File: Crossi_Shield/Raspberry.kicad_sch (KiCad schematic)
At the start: 12 parts, among them J1 Raspberry_Pi_2_3, SW1 SW_DIP_x01

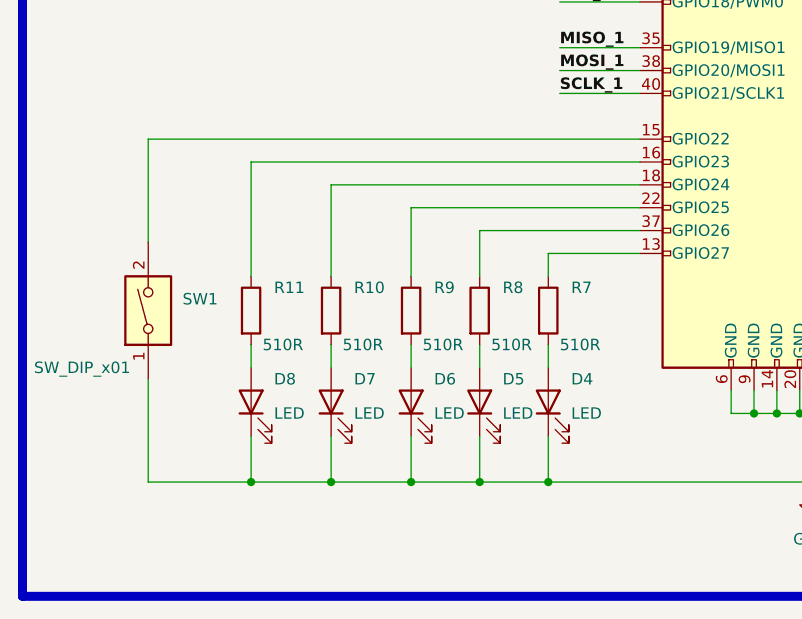
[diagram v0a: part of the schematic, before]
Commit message: new buckconf design
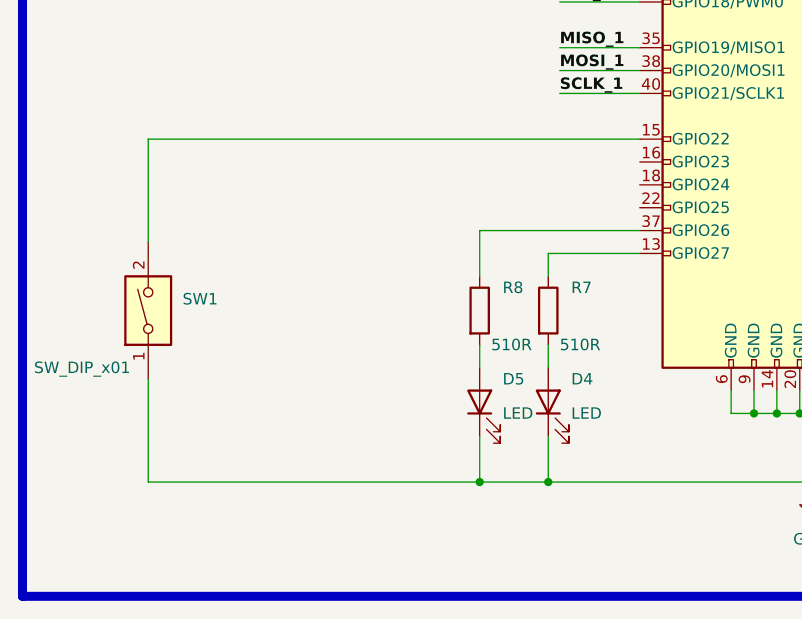
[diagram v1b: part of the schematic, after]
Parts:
- removed D6, D7, D8: LED, LED_SMD:LED_0805_2012Metric_Pad1.15x1.40mm_HandSolder, symbol Device:LED
- removed R10, R11, R9: 510R, Resistor_SMD:R_0805_2012Metric_Pad1.20x1.40mm_HandSolder, symbol Device:R
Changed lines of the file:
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@@
   (junction (at 99.06 138.43) (diameter 0) (color 0 0 0 0)
   )
-  (junction (at 74.93 138.43) (diameter 0) (color 0 0 0 0)
-  )
   (junction (at 127 130.81) (diameter 0) (color 0 0 0 0)
   )
-  (junction (at 66.04 138.43) (diameter 0) (color 0 0 0 0)
-  )
   (junction (at 124.46 130.81) (diameter 0) (color 0 0 0 0)
   )
@@
   (junction (at 128.27 130.81) (diameter 0) (color 0 0 0 0)
   )
-  (junction (at 83.82 138.43) (diameter 0) (color 0 0 0 0)
-  )
   (junction (at 121.92 130.81) (diameter 0) (color 0 0 0 0)
   )
@@
   (junction (at 129.54 130.81) (diameter 0) (color 0 0 0 0)
   )
-  (wire (pts (xy 109.22 105.41) (xy 74.93 105.41))
-    (stroke (width 0) (type default))
-  )
   (wire (pts (xy 223.52 78.74) (xy 232.41 78.74))
     (stroke (width 0) (type default))
@@
     (stroke (width 0) (type default))
   )
-  (wire (pts (xy 66.04 138.43) (xy 74.93 138.43))
-    (stroke (width 0) (type default))
-  )
   (wire (pts (xy 200.66 78.74) (xy 210.82 78.74))
     (stroke (width 0) (type default))
   )
-  (wire (pts (xy 83.82 107.95) (xy 83.82 115.57))
-    (stroke (width 0) (type default))
-  )
   (wire (pts (xy 223.52 86.36) (xy 232.41 86.36))
     (stroke (width 0) (type default))
@@
     (stroke (width 0) (type default))
   )
-  (wire (pts (xy 74.93 138.43) (xy 83.82 138.43))
-    (stroke (width 0) (type default))
-  )
   (wire (pts (xy 200.66 86.36) (xy 207.01 86.36))
     (stroke (width 0) (type default))
@@
     (stroke (width 0) (type default))
   )
-  (wire (pts (xy 83.82 123.19) (xy 83.82 125.73))
-    (stroke (width 0) (type default))
-  )
-  (wire (pts (xy 83.82 138.43) (xy 91.44 138.43))
+  (wire (pts (xy 54.61 138.43) (xy 91.44 138.43))
     (stroke (width 0) (type default))
   )
@@
     (stroke (width 0) (type default))
   )
-  (wire (pts (xy 66.04 123.19) (xy 66.04 125.73))
-    (stroke (width 0) (type default))
-  )
-  (wire (pts (xy 83.82 133.35) (xy 83.82 138.43))
-    (stroke (width 0) (type default))
-  )
-  (wire (pts (xy 54.61 138.43) (xy 66.04 138.43))
-    (stroke (width 0) (type default))
-  )
   (wire (pts (xy 149.86 100.33) (xy 158.75 100.33))
     (stroke (width 0) (type default))
@@
     (stroke (width 0) (type default))
   )
-  (wire (pts (xy 74.93 105.41) (xy 74.93 115.57))
-    (stroke (width 0) (type default))
-  )
   (wire (pts (xy 149.86 97.79) (xy 158.75 97.79))
     (stroke (width 0) (type default))
@@
     (stroke (width 0) (type default))
   )
-  (wire (pts (xy 74.93 123.19) (xy 74.93 125.73))
-    (stroke (width 0) (type default))
-  )
   (wire (pts (xy 149.86 80.01) (xy 156.21 80.01))
     (stroke (width 0) (type default))
@@
     (stroke (width 0) (type default))
   )
-  (wire (pts (xy 66.04 133.35) (xy 66.04 138.43))
-    (stroke (width 0) (type default))
-  )
   (wire (pts (xy 134.62 128.27) (xy 134.62 130.81))
     (stroke (width 0) (type default))
@@
     (stroke (width 0) (type default))
   )
-  (wire (pts (xy 109.22 107.95) (xy 83.82 107.95))
-    (stroke (width 0) (type default))
-  )
   (wire (pts (xy 200.66 68.58) (xy 207.01 68.58))
     (stroke (width 0) (type default))
@@
     (stroke (width 0) (type default))
   )
-  (wire (pts (xy 66.04 102.87) (xy 66.04 115.57))
-    (stroke (width 0) (type default))
-  )
   (wire (pts (xy 124.46 128.27) (xy 124.46 130.81))
     (stroke (width 0) (type default))
@@
     (stroke (width 0) (type default))
   )
-  (wire (pts (xy 109.22 102.87) (xy 66.04 102.87))
-    (stroke (width 0) (type default))
-  )
   (wire (pts (xy 149.86 72.39) (xy 156.21 72.39))
     (stroke (width 0) (type default))
@@
   )
   (wire (pts (xy 99.06 138.43) (xy 128.27 138.43))
-    (stroke (width 0) (type default))
-  )
-  (wire (pts (xy 74.93 133.35) (xy 74.93 138.43))
     (stroke (width 0) (type default))
   )
@@
         (path "/da1a3662-bd33-45fa-9d2c-eaee6b865c8d/f28ea0f3-753b-42f3-99ad-0aa8f46314aa"
           (reference "D5") (unit 1)
-        )
-      )
-    )
-  )
-  (symbol (lib_id "Device:R") (at 74.93 119.38 0) (unit 1)
-    (in_bom yes) (on_board yes) (dnp no)
-    (property "Reference" "R10" (at 77.47 116.84 0)
-      (effects (font (size 1.27 1.27)) (justify left))
-    )
-    (property "Value" "510R" (at 76.2 123.19 0)
-      (effects (font (size 1.27 1.27)) (justify left))
-    )
-    (property "Footprint" "Resistor_SMD:R_0805_2012Metric_Pad1.20x1.40mm_HandSolder" (at 73.152 119.38 90)
-      (effects (font (size 1.27 1.27)) hide)
-    )
-    (property "Datasheet" "~" (at 74.93 119.38 0)
-      (effects (font (size 1.27 1.27)) hide)
-    )
-    (pin "1")
-    (pin "2")
-    (instances
-      (project "Crossi_Shield"
-        (path "/da1a3662-bd33-45fa-9d2c-eaee6b865c8d/f28ea0f3-753b-42f3-99ad-0aa8f46314aa"
-          (reference "R10") (unit 1)
         )
       )
@@
     )
   )
-  (symbol (lib_id "Device:LED") (at 74.93 129.54 90) (unit 1)
-    (in_bom yes) (on_board yes) (dnp no)
-    (property "Reference" "D7" (at 77.47 127 90)
-      (effects (font (size 1.27 1.27)) (justify right))
-    )
-    (property "Value" "LED" (at 77.47 130.81 90)
-      (effects (font (size 1.27 1.27)) (justify right))
-    )
-    (property "Footprint" "LED_SMD:LED_0805_2012Metric_Pad1.15x1.40mm_HandSolder" (at 74.93 129.54 0)
-      (effects (font (size 1.27 1.27)) hide)
-    )
-    (property "Datasheet" "~" (at 74.93 129.54 0)
-      (effects (font (size 1.27 1.27)) hide)
-    )
-    (pin "1")
-    (pin "2")
-    (instances
-      (project "Crossi_Shield"
-        (path "/da1a3662-bd33-45fa-9d2c-eaee6b865c8d/f28ea0f3-753b-42f3-99ad-0aa8f46314aa"
-          (reference "D7") (unit 1)
-        )
-      )
-    )
-  )
-  (symbol (lib_id "Device:R") (at 83.82 119.38 0) (unit 1)
-    (in_bom yes) (on_board yes) (dnp no)
-    (property "Reference" "R9" (at 86.36 116.84 0)
-      (effects (font (size 1.27 1.27)) (justify left))
-    )
-    (property "Value" "510R" (at 85.09 123.19 0)
-      (effects (font (size 1.27 1.27)) (justify left))
-    )
-    (property "Footprint" "Resistor_SMD:R_0805_2012Metric_Pad1.20x1.40mm_HandSolder" (at 82.042 119.38 90)
-      (effects (font (size 1.27 1.27)) hide)
-    )
-    (property "Datasheet" "~" (at 83.82 119.38 0)
-      (effects (font (size 1.27 1.27)) hide)
-    )
-    (pin "1")
-    (pin "2")
-    (instances
-      (project "Crossi_Shield"
-        (path "/da1a3662-bd33-45fa-9d2c-eaee6b865c8d/f28ea0f3-753b-42f3-99ad-0aa8f46314aa"
-          (reference "R9") (unit 1)
-        )
-      )
-    )
-  )
-  (symbol (lib_id "Device:LED") (at 83.82 129.54 90) (unit 1)
-    (in_bom yes) (on_board yes) (dnp no)
-    (property "Reference" "D6" (at 86.36 127 90)
-      (effects (font (size 1.27 1.27)) (justify right))
-    )
-    (property "Value" "LED" (at 86.36 130.81 90)
-      (effects (font (size 1.27 1.27)) (justify right))
-    )
-    (property "Footprint" "LED_SMD:LED_0805_2012Metric_Pad1.15x1.40mm_HandSolder" (at 83.82 129.54 0)
-      (effects (font (size 1.27 1.27)) hide)
-    )
-    (property "Datasheet" "~" (at 83.82 129.54 0)
-      (effects (font (size 1.27 1.27)) hide)
-    )
-    (pin "1")
-    (pin "2")
-    (instances
-      (project "Crossi_Shield"
-        (path "/da1a3662-bd33-45fa-9d2c-eaee6b865c8d/f28ea0f3-753b-42f3-99ad-0aa8f46314aa"
-          (reference "D6") (unit 1)
-        )
-      )
-    )
-  )
   (symbol (lib_id "Device:R") (at 99.06 119.38 0) (unit 1)
     (in_bom yes) (on_board yes) (dnp no)
@@
     )
   )
-  (symbol (lib_id "Device:LED") (at 66.04 129.54 90) (unit 1)
-    (in_bom yes) (on_board yes) (dnp no)
-    (property "Reference" "D8" (at 68.58 127 90)
-      (effects (font (size 1.27 1.27)) (justify right))
-    )
-    (property "Value" "LED" (at 68.58 130.81 90)
-      (effects (font (size 1.27 1.27)) (justify right))
-    )
-    (property "Footprint" "LED_SMD:LED_0805_2012Metric_Pad1.15x1.40mm_HandSolder" (at 66.04 129.54 0)
-      (effects (font (size 1.27 1.27)) hide)
-    )
-    (property "Datasheet" "~" (at 66.04 129.54 0)
-      (effects (font (size 1.27 1.27)) hide)
-    )
-    (pin "1")
-    (pin "2")
-    (instances
-      (project "Crossi_Shield"
-        (path "/da1a3662-bd33-45fa-9d2c-eaee6b865c8d/f28ea0f3-753b-42f3-99ad-0aa8f46314aa"
-          (reference "D8") (unit 1)
-        )
-      )
-    )
-  )
   (symbol (lib_id "Switch:SW_DIP_x01") (at 54.61 119.38 90) (unit 1)
     (in_bom yes) (on_board yes) (dnp no)
@@
         )
       )
-    )
-  )
-  (symbol (lib_id "Device:R") (at 66.04 119.38 0) (unit 1)
-    (in_bom yes) (on_board yes) (dnp no)
-    (property "Reference" "R11" (at 68.58 116.84 0)
-      (effects (font (size 1.27 1.27)) (justify left))
-    )
-    (property "Value" "510R" (at 67.31 123.19 0)
-      (effects (font (size 1.27 1.27)) (justify left))
-    )
-    (property "Footprint" "Resistor_SMD:R_0805_2012Metric_Pad1.20x1.40mm_HandSolder" (at 64.262 119.38 90)
-      (effects (font (size 1.27 1.27)) hide)
-    )
-    (property "Datasheet" "~" (at 66.04 119.38 0)
-      (effects (font (size 1.27 1.27)) hide)
-    )
-    (pin "1")
-    (pin "2")
-    (instances
-      (project "Crossi_Shield"
-        (path "/da1a3662-bd33-45fa-9d2c-eaee6b865c8d/f28ea0f3-753b-42f3-99ad-0aa8f46314aa"
-          (reference "R11") (unit 1)
-        )
-      )
